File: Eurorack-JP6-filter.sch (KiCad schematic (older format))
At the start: 138 parts, among them J1 JACK_MONO_SW, J2 JACK_MONO_SW, J3 JACK_MONO_SW, J4 JACK_MONO_SW, J5 JACK_MONO_SW, J6 JACK_MONO_SW, P1 CONN_02X05, Q1 BCM857BS, Q2 BCM857BS, Q3 J112, Q4 J112, Q5 J112, Q6 J112, SW1 KS-01Q, U1 TL072-, U10 CD4027, U11 CD40106, U2 TL072-, U3 TL072-, U4 TL072-, U5 LM13700, U6 LM13700, U7 LM13700, U8 DG409, U9 CD4052

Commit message: finished routing, mostly cleaned upk, parts modelled in 5365
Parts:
- Q1, Q2: footprint synth:SOT363-JRL -> MyModules:SOT363-JRL
- U5, U6, U7, U8: footprint synth:SO16-JRL -> MyModules:SO16-JRL
- VR1, VR2, VR3, VR4, VR6: footprint synth:RV16A-41-JRL -> MyModules:RV16A-41-JRL
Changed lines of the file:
@@
 F 0 "U5" H 7850 11100 60  0000 C CNN
 F 1 "LM13700" H 7650 11300 60  0000 C CNN
-F 2 "synth:SO16-JRL" H 7750 11300 60  0001 C CNN
+F 2 "MyModules:SO16-JRL" H 7750 11300 60  0001 C CNN
 F 3 "" H 7750 11300 60  0000 C CNN
 	1    7750 11300
@@
 F 0 "Q2" H 6600 2950 60  0000 R CNN
 F 1 "BCM857BS" H 6950 2500 60  0000 R CNN
-F 2 "synth:SOT363-JRL" H 6100 2700 60  0001 C CNN
+F 2 "MyModules:SOT363-JRL" H 6100 2700 60  0001 C CNN
 F 3 "" H 6100 2700 60  0000 C CNN
 	1    6300 2700
@@
 F 0 "VR1" H 950 3500 50  0000 C CNN
 F 1 "50K" H 950 3570 50  0000 C CNN
-F 2 "synth:RV16A-41-JRL" H 950 3650 60  0001 C CNN
+F 2 "MyModules:RV16A-41-JRL" H 950 3650 60  0001 C CNN
 F 3 "" H 950 3650 60  0000 C CNN
 	1    950  3650
@@
 F 0 "VR4" H 2250 2700 50  0000 C CNN
 F 1 "50K" H 2250 2770 50  0000 C CNN
-F 2 "synth:RV16A-41-JRL" H 2250 2850 60  0001 C CNN
+F 2 "MyModules:RV16A-41-JRL" H 2250 2850 60  0001 C CNN
 F 3 "" H 2250 2850 60  0000 C CNN
 	1    2250 2850
@@
 F 0 "VR3" H 2250 1850 50  0000 C CNN
 F 1 "50K" H 2250 1920 50  0000 C CNN
-F 2 "synth:RV16A-41-JRL" H 2250 2000 60  0001 C CNN
+F 2 "MyModules:RV16A-41-JRL" H 2250 2000 60  0001 C CNN
 F 3 "" H 2250 2000 60  0000 C CNN
 	1    2250 2000
@@
 F 0 "Q1" H 5100 6550 60  0000 R CNN
 F 1 "BCM857BS" H 5450 6100 60  0000 R CNN
-F 2 "synth:SOT363-JRL" H 4600 6300 60  0001 C CNN
+F 2 "MyModules:SOT363-JRL" H 4600 6300 60  0001 C CNN
 F 3 "" H 4600 6300 60  0000 C CNN
 	1    4800 6300
@@
 F 0 "VR2" H 950 6250 50  0000 C CNN
 F 1 "50K" H 950 6320 50  0000 C CNN
-F 2 "synth:RV16A-41-JRL" H 950 6400 60  0001 C CNN
+F 2 "MyModules:RV16A-41-JRL" H 950 6400 60  0001 C CNN
 F 3 "" H 950 6400 60  0000 C CNN
 	1    950  6400
@@
 F 0 "VR6" H 2350 10600 50  0000 C CNN
 F 1 "50K" H 2350 10670 50  0000 C CNN
-F 2 "synth:RV16A-41-JRL" H 2350 10750 60  0001 C CNN
+F 2 "MyModules:RV16A-41-JRL" H 2350 10750 60  0001 C CNN
 F 3 "" H 2350 10750 60  0000 C CNN
 	1    2350 10750
@@
 F 0 "U5" H 10450 11100 60  0000 C CNN
 F 1 "LM13700" H 10250 11300 60  0000 C CNN
-F 2 "synth:SO16-JRL" H 10350 11300 60  0001 C CNN
+F 2 "MyModules:SO16-JRL" H 10350 11300 60  0001 C CNN
 F 3 "" H 10350 11300 60  0000 C CNN
 	2    10350 11300
@@
 F 0 "U6" H 8050 9700 60  0000 C CNN
 F 1 "LM13700" H 7850 9900 60  0000 C CNN
-F 2 "synth:SO16-JRL" H 7950 9900 60  0001 C CNN
+F 2 "MyModules:SO16-JRL" H 7950 9900 60  0001 C CNN
 F 3 "" H 7950 9900 60  0000 C CNN
 	1    7950 9900
@@
 F 0 "U7" H 18750 11100 60  0000 C CNN
 F 1 "LM13700" H 18550 11300 60  0000 C CNN
-F 2 "synth:SO16-JRL" H 18650 11300 60  0001 C CNN
+F 2 "MyModules:SO16-JRL" H 18650 11300 60  0001 C CNN
 F 3 "" H 18650 11300 60  0000 C CNN
 	1    18650 11300
@@
 F 0 "U7" H 16150 11100 60  0000 C CNN
 F 1 "LM13700" H 15950 11300 60  0000 C CNN
-F 2 "synth:SO16-JRL" H 16050 11300 60  0001 C CNN
+F 2 "MyModules:SO16-JRL" H 16050 11300 60  0001 C CNN
 F 3 "" H 16050 11300 60  0000 C CNN
 	2    16050 11300
@@
 F 0 "U6" H 16350 9700 60  0000 C CNN
 F 1 "LM13700" H 16150 9900 60  0000 C CNN
-F 2 "synth:SO16-JRL" H 16250 9900 60  0001 C CNN
+F 2 "MyModules:SO16-JRL" H 16250 9900 60  0001 C CNN
 F 3 "" H 16250 9900 60  0000 C CNN
 	2    16250 9900
@@
 F 0 "U8" H 10550 3750 60  0000 C CNN
 F 1 "DG409" H 11150 3750 60  0000 C CNN
-F 2 "synth:SO16-JRL" H 10900 3050 60  0001 C CNN
+F 2 "MyModules:SO16-JRL" H 10900 3050 60  0001 C CNN
 F 3 "" H 10900 3050 60  0000 C CNN
 	1    10900 3050

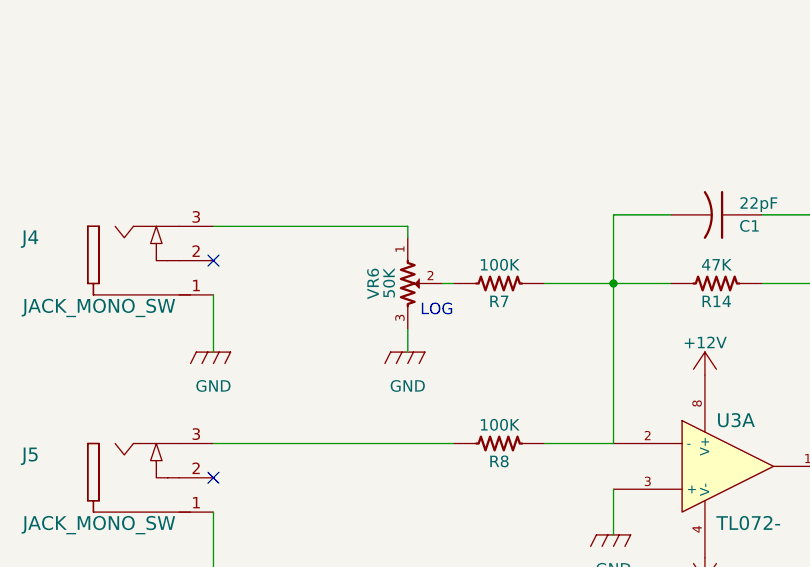
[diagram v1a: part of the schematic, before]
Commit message: anode cathode diode swap from latest kicad library updates fixed, ground plane tweaking
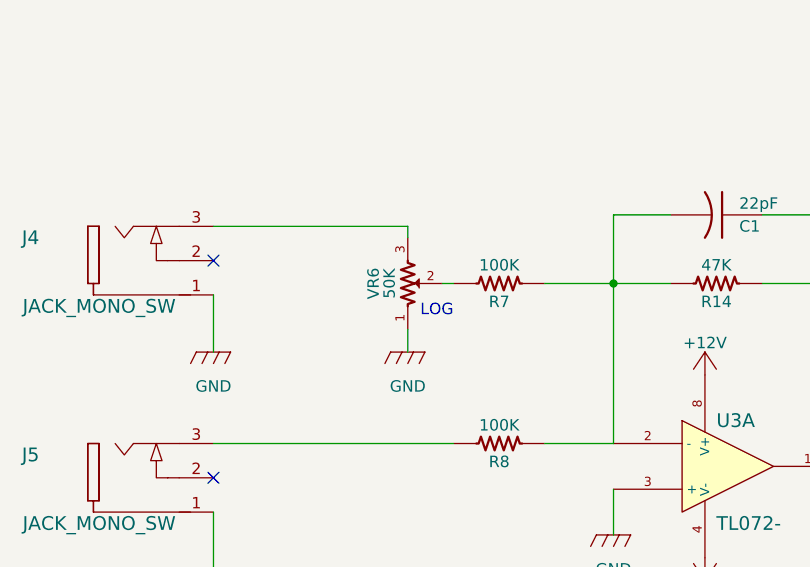
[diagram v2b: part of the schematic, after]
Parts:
- D1, D2, D3, D4: footprint MyModules:3MM-LED -> MyModules:3MM-LED-C1A2
- D5, D6, D7: footprint MyModules:SOD323-JRL -> MyModules:SOD323-C1A2
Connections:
- net GND: now also VR6.1; no longer VR6.3
- net at J4.3: now also VR6.3; no longer VR6.1
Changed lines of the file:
@@
 F 3 "" H 2350 10750 60  0000 C CNN
 	1    2350 10750
-	0    1    1    0
+	0    1    -1   0
 $EndComp
 $Comp
@@
 F 0 "D5" H 14150 12300 50  0000 C CNN
 F 1 "1N914" H 14150 12100 50  0000 C CNN
-F 2 "MyModules:SOD323-JRL" H 14150 12200 60  0001 C CNN
+F 2 "MyModules:SOD323-C1A2" H 14150 12200 60  0001 C CNN
 F 3 "" H 14150 12200 60  0000 C CNN
 	1    14150 12200
@@
 F 0 "D6" H 14150 12550 50  0000 C CNN
 F 1 "1N914" H 14150 12350 50  0000 C CNN
-F 2 "MyModules:SOD323-JRL" H 14150 12450 60  0001 C CNN
+F 2 "MyModules:SOD323-C1A2" H 14150 12450 60  0001 C CNN
 F 3 "" H 14150 12450 60  0000 C CNN
 	1    14150 12450
@@
 F 0 "D1" H 9000 4850 50  0000 C CNN
 F 1 "LED" H 9450 4850 50  0000 C CNN
-F 2 "MyModules:3MM-LED" H 9200 4800 60  0001 C CNN
+F 2 "MyModules:3MM-LED-C1A2" H 9200 4800 60  0001 C CNN
 F 3 "" H 9200 4800 60  0000 C CNN
 	1    9200 4800
@@
 F 0 "D2" H 9000 5100 50  0000 C CNN
 F 1 "LED" H 9450 5100 50  0000 C CNN
-F 2 "MyModules:3MM-LED" H 9200 5050 60  0001 C CNN
+F 2 "MyModules:3MM-LED-C1A2" H 9200 5050 60  0001 C CNN
 F 3 "" H 9200 5050 60  0000 C CNN
 	1    9200 5050
@@
 F 0 "D3" H 9000 5350 50  0000 C CNN
 F 1 "LED" H 9450 5350 50  0000 C CNN
-F 2 "MyModules:3MM-LED" H 9200 5300 60  0001 C CNN
+F 2 "MyModules:3MM-LED-C1A2" H 9200 5300 60  0001 C CNN
 F 3 "" H 9200 5300 60  0000 C CNN
 	1    9200 5300
@@
 F 0 "D4" H 9000 5600 50  0000 C CNN
 F 1 "LED" H 9450 5600 50  0000 C CNN
-F 2 "MyModules:3MM-LED" H 9200 5550 60  0001 C CNN
+F 2 "MyModules:3MM-LED-C1A2" H 9200 5550 60  0001 C CNN
 F 3 "" H 9200 5550 60  0000 C CNN
 	1    9200 5550
@@
 F 0 "D7" H 17850 6450 50  0000 C CNN
 F 1 "1N914" H 17850 6250 50  0000 C CNN
-F 2 "MyModules:SOD323-JRL" H 17850 6350 60  0001 C CNN
+F 2 "MyModules:SOD323-C1A2" H 17850 6350 60  0001 C CNN
 F 3 "" H 17850 6350 60  0000 C CNN
 	1    17850 6350

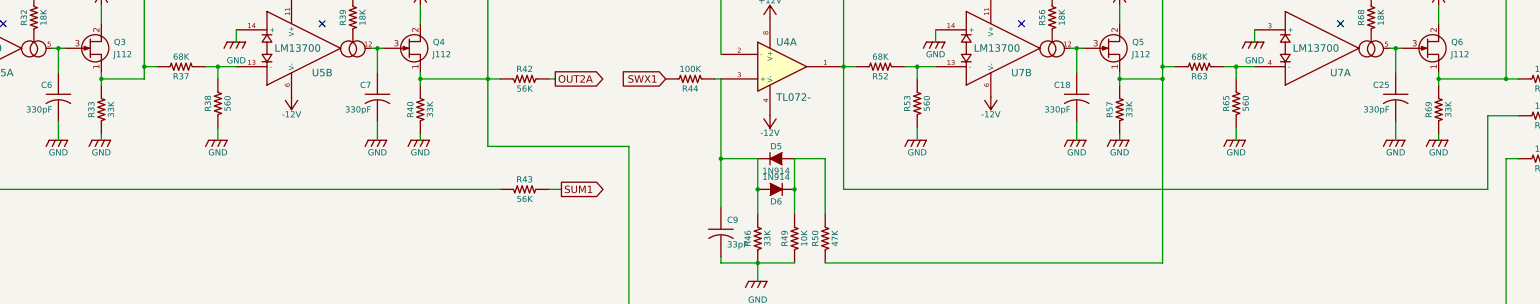
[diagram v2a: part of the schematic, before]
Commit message: JFET buffer 33K R to GND error fixed to -12V
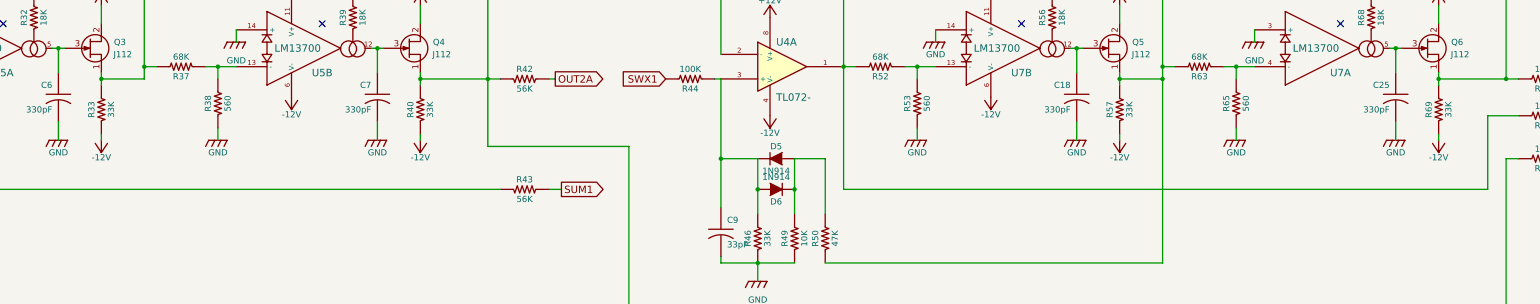
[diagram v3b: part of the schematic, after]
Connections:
- net -12V: now also R33.1, R40.1, R57.1, R69.1
- net GND: no longer R33.1, R40.1, R57.1, R69.1

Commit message: clean up duplicate versions of Gerbers, add Panel folder for panel fab and screen graphics
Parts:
- Q3, Q4, Q5, Q6: symbol Q_NJFET_SDG -> Q_NJFET_SDG-RESCUE-Eurorack-JP6-filter
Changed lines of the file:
@@
 EESchema Schematic File Version 2
+LIBS:Eurorack-JP6-filter-rescue
 LIBS:MySynthParts
 LIBS:power
@@
 LIBS:memory
 LIBS:xilinx
-LIBS:special
 LIBS:microcontrollers
 LIBS:dsp
@@
 NoConn ~ 15850 15450
 $Comp
-L Q_NJFET_SDG Q6
+L Q_NJFET_SDG-RESCUE-Eurorack-JP6-filter Q6
 U 1 1 554F0331
 P 19450 11300
@@
 $EndComp
 $Comp
-L Q_NJFET_SDG Q5
+L Q_NJFET_SDG-RESCUE-Eurorack-JP6-filter Q5
 U 1 1 554F0714
 P 16850 11300
@@
 $EndComp
 $Comp
-L Q_NJFET_SDG Q4
+L Q_NJFET_SDG-RESCUE-Eurorack-JP6-filter Q4
 U 1 1 554F0CB3
 P 11150 11300
@@
 $EndComp
 $Comp
-L Q_NJFET_SDG Q3
+L Q_NJFET_SDG-RESCUE-Eurorack-JP6-filter Q3
 U 1 1 554F15DD
 P 8550 11300

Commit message: changed power-on-reset R61 resistor to 100K for more reliable POR
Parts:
- R61: value 33K -> 100K

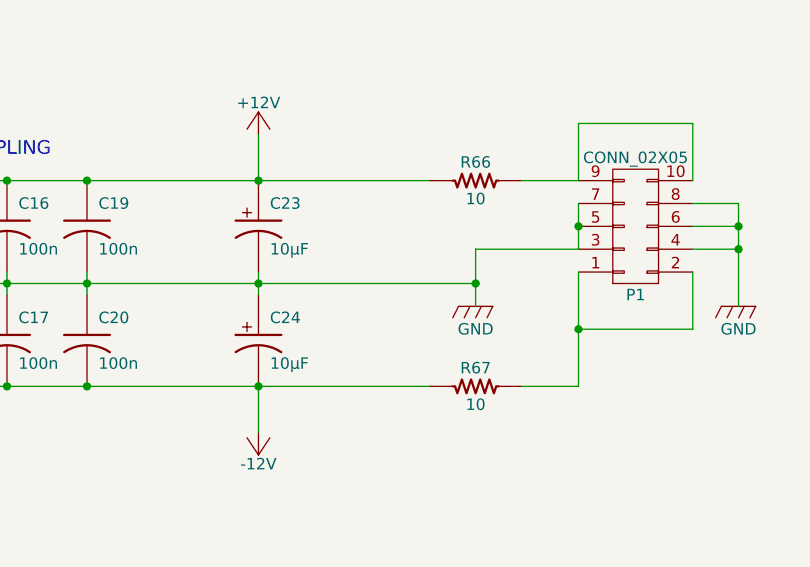
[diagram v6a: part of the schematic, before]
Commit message: Power polarity protection diodes added, TSSOP-8 footprints changed to KiCad standard, removal of references to VRML1 models, Gerber plots updated
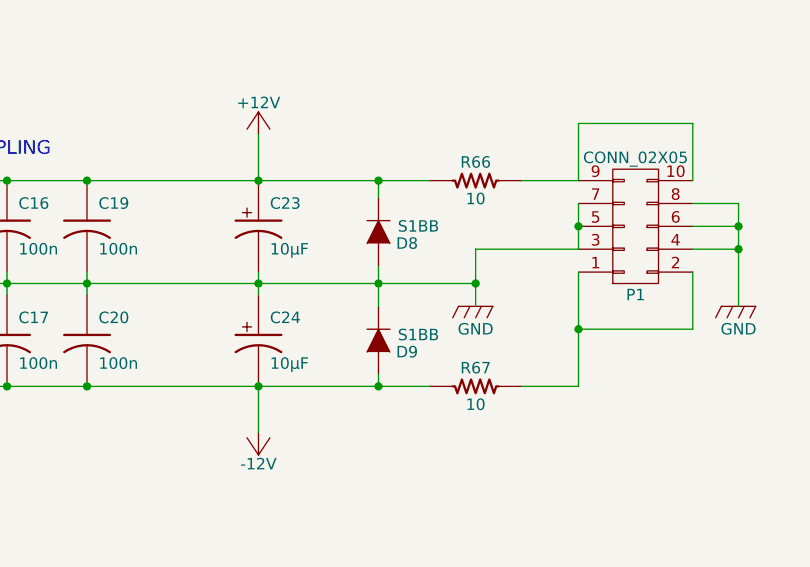
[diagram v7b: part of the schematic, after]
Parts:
- added D8, D9: S1BB, MyModules:SMB-1C2A, symbol D
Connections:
- net +12V: now also D8.1 (K)
- net -12V: now also D9.2 (A)
- net GND: now also D8.2 (A), D9.1 (K)
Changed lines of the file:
@@
 	-1   0    0    1
 $EndComp
+$Comp
+L D D8
+U 1 1 57242018
+P 18175 1625
+F 0 "D8" V 18225 1750 50  0000 C CNN
+F 1 "S1BB" V 18150 1800 50  0000 C CNN
+F 2 "MyModules:SMB-1C2A" H 18175 1625 60  0001 C CNN
+F 3 "" H 18175 1625 60  0000 C CNN
+	1    18175 1625
+	0    1    1    0
+$EndComp
+Wire Wire Line
+	18175 1475 18175 1400
+Connection ~ 18175 1400
+Wire Wire Line
+	18175 1775 18175 1950
+Connection ~ 18175 1850
+$Comp
+L D D9
+U 1 1 57244C3A
+P 18175 2100
+F 0 "D9" V 18225 2225 50  0000 C CNN
+F 1 "S1BB" V 18150 2275 50  0000 C CNN
+F 2 "MyModules:SMB-1C2A" H 18175 2100 60  0001 C CNN
+F 3 "" H 18175 2100 60  0000 C CNN
+	1    18175 2100
+	0    1    1    0
+$EndComp
+Wire Wire Line
+	18175 2250 18175 2300
+Connection ~ 18175 2300
 $EndSCHEMATC

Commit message: changed CV2 intput to attenuverter
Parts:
- removed R4: 100K, MyModules:SM0603-R-JRL, symbol R_US
- added R? (x4): 100K, MyModules:SM0603-R-JRL, symbol R_US
- added U?: TL072-, MyModules:TSSOP8-JRL, symbol TL072-
- added VR?: 50K, MyModules:RV16A-41-JRL, symbol POT_US
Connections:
- net GND: now also VR4.2; no longer VR4.1
- net at R10.1, R13.2, R2.1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: now also R?.1
- net at VR4.3: now also VR?.1; no longer J3.3
- new net: R?.1, U?.3 (+), VR4.1
- new net: J3.3, R?.2, R?.2
- new net: R?.1, R?.2, U?.1
- new net: R?.2, U?.2 (-), VR?.2, VR?.3
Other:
- moved on the sheet: C21, C22, C5, D1, D2, D3, D4, D7, J1, J2, J3, Q2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
